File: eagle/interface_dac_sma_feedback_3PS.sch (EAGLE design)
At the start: 36 parts, among them IC1 ISO1540, IC2 LT1352PA, IC3 LT1352PA, Q1 TIP122V, Q2 TIP122V, Q3 TIP122V, X1 BU-SMA-V

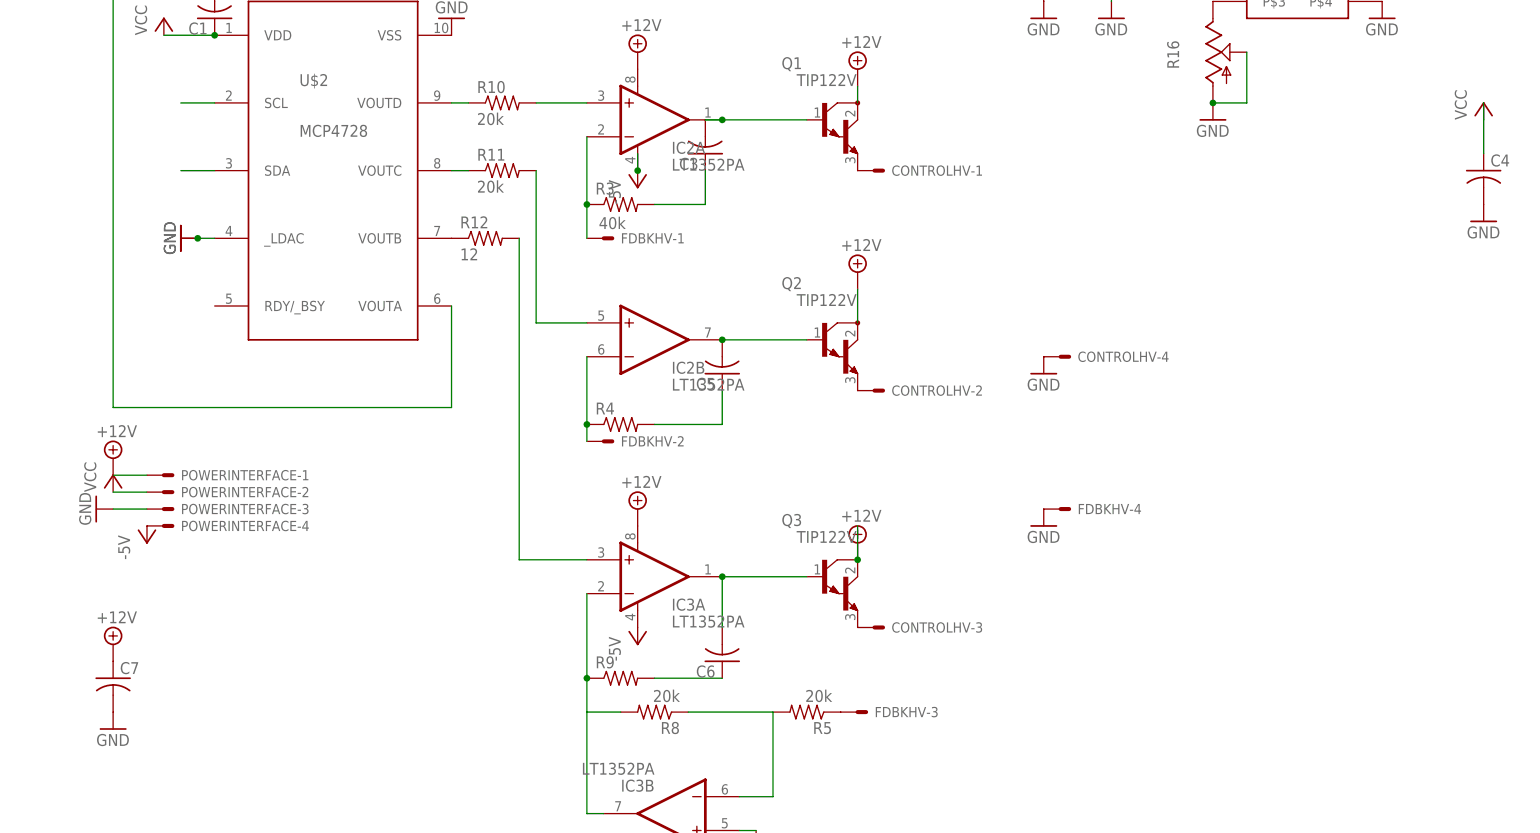
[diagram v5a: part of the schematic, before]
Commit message: update component values
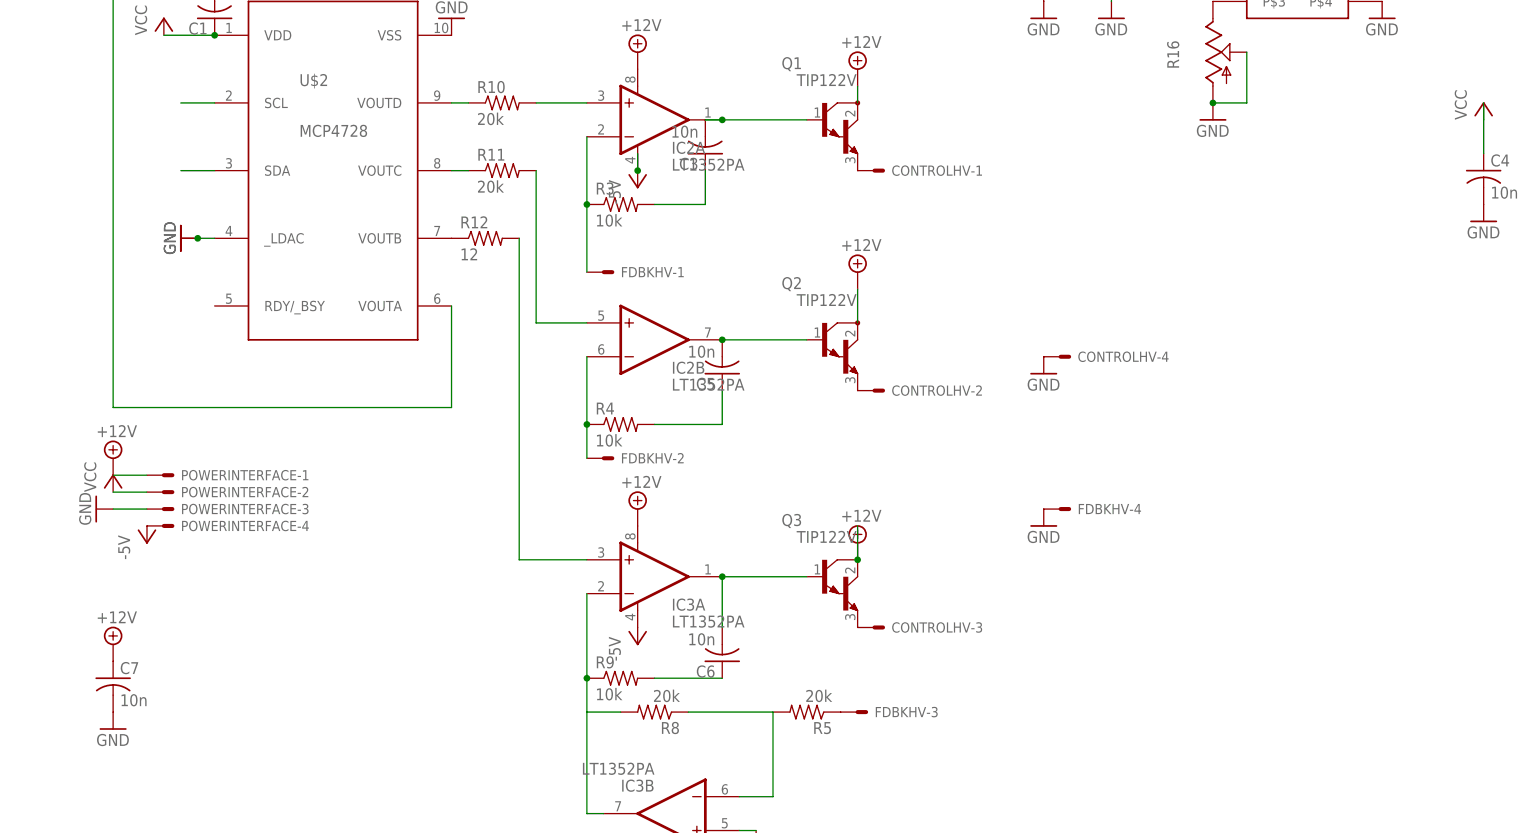
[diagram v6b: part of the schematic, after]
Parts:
- C3, C4, C5, C6, C7: value (none) -> 10n
- FDBKHV: value 40k -> (none)
- R3, R4, R9: value (none) -> 10k
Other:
- moved on the sheet: FDBKHV-1, FDBKHV-2
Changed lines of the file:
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@@
 <part name="P+2" library="supply2" deviceset="+12V" device=""/>
 <part name="U$1" library="linear-technology" deviceset="LTC6992" device=""/>
-<part name="C4" library="resistor" deviceset="C-US" device="075-063X106"/>
+<part name="C4" library="resistor" deviceset="C-US" device="075-063X106" value="10n"/>
 <part name="R16" library="pot" deviceset="TRIM_US-" device="B90P"/>
 <part name="GND13" library="supply1" deviceset="GND" device=""/>
@@
 <part name="P+8" library="supply2" deviceset="+12V" device=""/>
 <part name="CONTROLHV" library="con-molex" deviceset="KK-156-4" device=""/>
-<part name="FDBKHV" library="con-molex" deviceset="KK-156-4" device="" value="40k"/>
+<part name="FDBKHV" library="con-molex" deviceset="KK-156-4" device=""/>
 <part name="GND2" library="supply1" deviceset="GND" device=""/>
 <part name="GND6" library="supply1" deviceset="GND" device=""/>
@@
 <part name="P-2" library="supply1" deviceset="-5V" device=""/>
 <part name="GND18" library="supply1" deviceset="GND" device=""/>
-<part name="R3" library="resistor" deviceset="R-US_" device="0207/12"/>
-<part name="C3" library="resistor" deviceset="C-US" device="050-024X044"/>
-<part name="R4" library="resistor" deviceset="R-US_" device="0207/12"/>
-<part name="C5" library="resistor" deviceset="C-US" device="050-024X044"/>
-<part name="R9" library="resistor" deviceset="R-US_" device="0207/12"/>
-<part name="C6" library="resistor" deviceset="C-US" device="050-024X044"/>
+<part name="R3" library="resistor" deviceset="R-US_" device="0207/12" value="10k"/>
+<part name="C3" library="resistor" deviceset="C-US" device="050-024X044" value="10n"/>
+<part name="R4" library="resistor" deviceset="R-US_" device="0207/12" value="10k"/>
+<part name="C5" library="resistor" deviceset="C-US" device="050-024X044" value="10n"/>
+<part name="R9" library="resistor" deviceset="R-US_" device="0207/12" value="10k"/>
+<part name="C6" library="resistor" deviceset="C-US" device="050-024X044" value="10n"/>
 <part name="P+14" library="supply2" deviceset="+12V" device=""/>
-<part name="C7" library="resistor" deviceset="C-US" device="050-050X075"/>
+<part name="C7" library="resistor" deviceset="C-US" device="050-050X075" value="10n"/>
 <part name="GND20" library="supply1" deviceset="GND" device=""/>
 <part name="R10" library="resistor" deviceset="R-US_" device="0207/12" value="20k"/>
@@
 <instance part="CONTROLHV" gate="-3" x="203.2" y="15.24"/>
 <instance part="CONTROLHV" gate="-4" x="231.14" y="55.88"/>
-<instance part="FDBKHV" gate="-1" x="162.56" y="73.66"/>
-<instance part="FDBKHV" gate="-2" x="162.56" y="43.18"/>
+<instance part="FDBKHV" gate="-1" x="162.56" y="68.58"/>
+<instance part="FDBKHV" gate="-2" x="162.56" y="40.64"/>
 <instance part="FDBKHV" gate="-3" x="200.66" y="2.54"/>
 <instance part="FDBKHV" gate="-4" x="231.14" y="33.02"/>
@@
 <pinref part="FDBKHV" gate="-1" pin="S"/>
 <pinref part="R3" gate="G$1" pin="1"/>
-<wire x1="160.02" y1="78.74" x2="160.02" y2="73.66" width="0.1524" layer="91"/>
+<wire x1="160.02" y1="78.74" x2="160.02" y2="68.58" width="0.1524" layer="91"/>
 <junction x="160.02" y="78.74"/>
 <pinref part="IC2" gate="A" pin="-IN"/>
@@
 <pinref part="FDBKHV" gate="-2" pin="S"/>
 <pinref part="R4" gate="G$1" pin="1"/>
-<wire x1="160.02" y1="45.72" x2="160.02" y2="43.18" width="0.1524" layer="91"/>
+<wire x1="160.02" y1="45.72" x2="160.02" y2="40.64" width="0.1524" layer="91"/>
 <junction x="160.02" y="45.72"/>
 <pinref part="IC2" gate="B" pin="-IN"/>

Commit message: Update values, code
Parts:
- R10, R11: value 20k -> 10k
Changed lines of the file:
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@@
 <part name="C7" library="resistor" deviceset="C-US" device="050-050X075" value="10n"/>
 <part name="GND20" library="supply1" deviceset="GND" device=""/>
-<part name="R10" library="resistor" deviceset="R-US_" device="0207/12" value="20k"/>
-<part name="R11" library="resistor" deviceset="R-US_" device="0207/12" value="20k"/>
+<part name="R10" library="resistor" deviceset="R-US_" device="0207/12" value="10k"/>
+<part name="R11" library="resistor" deviceset="R-US_" device="0207/12" value="10k"/>
 <part name="R12" library="resistor" deviceset="R-US_" device="0207/12" value="12"/>
 <part name="Q1" library="transistor-npn" deviceset="TIP122*" device="V"/>

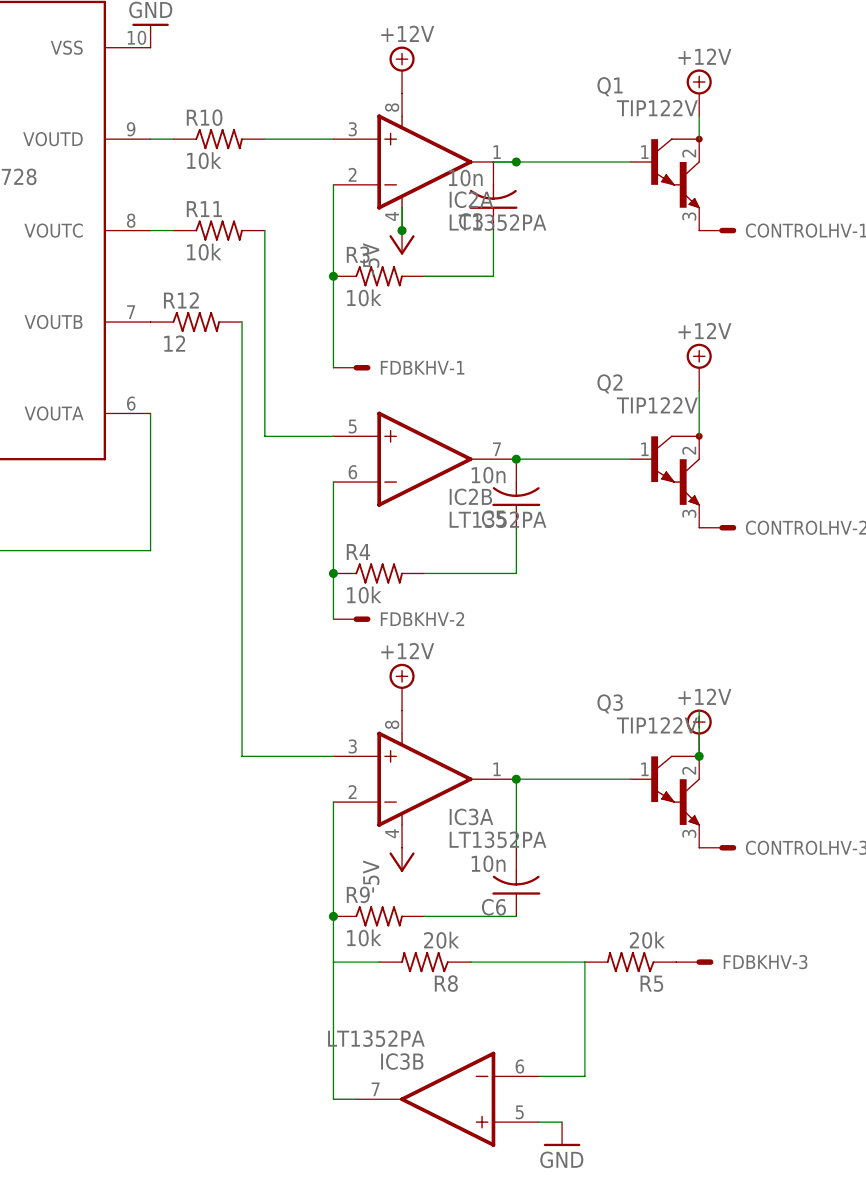
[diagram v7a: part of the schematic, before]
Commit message: Fix negative rail problems
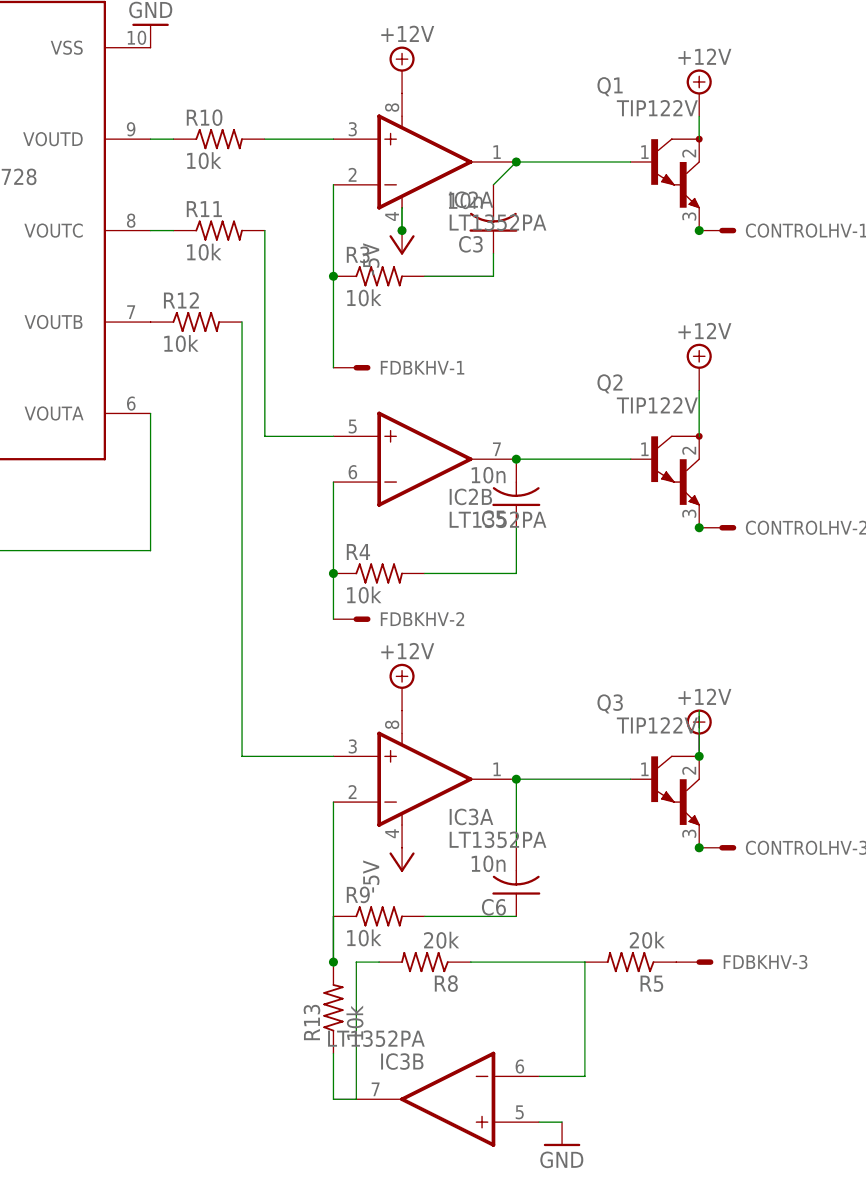
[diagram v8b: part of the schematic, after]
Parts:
- added R13: 10k, resistor:R-US_0207/12
- R12: value 12 -> 10k
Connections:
- new net N$27: IC3A.-IN, R13.2, R9.1
- net N$14: now also R13.1; no longer IC3A.-IN, R9.1
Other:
- moved on the sheet: C3
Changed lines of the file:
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@@
 <part name="R10" library="resistor" deviceset="R-US_" device="0207/12" value="10k"/>
 <part name="R11" library="resistor" deviceset="R-US_" device="0207/12" value="10k"/>
-<part name="R12" library="resistor" deviceset="R-US_" device="0207/12" value="12"/>
+<part name="R12" library="resistor" deviceset="R-US_" device="0207/12" value="10k"/>
 <part name="Q1" library="transistor-npn" deviceset="TIP122*" device="V"/>
 <part name="Q2" library="transistor-npn" deviceset="TIP122*" device="V"/>
@@
 <part name="IC3" library="linear-technology" deviceset="LT1352" device="PA"/>
 <part name="P-3" library="supply1" deviceset="-5V" device=""/>
+<part name="R13" library="resistor" deviceset="R-US_" device="0207/12" value="10k"/>
 </parts>
 <sheets>
@@
 <instance part="GND18" gate="1" x="185.42" y="-17.78"/>
 <instance part="R3" gate="G$1" x="165.1" y="78.74"/>
-<instance part="C3" gate="G$1" x="177.8" y="86.36" rot="R180"/>
+<instance part="C3" gate="G$1" x="177.8" y="83.82" rot="R180"/>
 <instance part="R4" gate="G$1" x="165.1" y="45.72"/>
 <instance part="C5" gate="G$1" x="180.34" y="53.34" rot="R180"/>
@@
 <instance part="IC3" gate="B" x="172.72" y="-12.7" rot="R180"/>
 <instance part="P-3" gate="1" x="167.64" y="81.28"/>
+<instance part="R13" gate="G$1" x="160.02" y="-2.54" rot="R90"/>
 </instances>
 <busses>
@@
 <segment>
 <wire x1="162.56" y1="-12.7" x2="160.02" y2="-12.7" width="0.1524" layer="91"/>
-<wire x1="160.02" y1="-12.7" x2="160.02" y2="2.54" width="0.1524" layer="91"/>
+<pinref part="IC3" gate="B" pin="OUT"/>
 <pinref part="R8" gate="G$1" pin="2"/>
-<wire x1="160.02" y1="2.54" x2="160.02" y2="7.62" width="0.1524" layer="91"/>
-<wire x1="160.02" y1="7.62" x2="160.02" y2="20.32" width="0.1524" layer="91"/>
-<wire x1="165.1" y1="2.54" x2="160.02" y2="2.54" width="0.1524" layer="91"/>
-<pinref part="R9" gate="G$1" pin="1"/>
-<junction x="160.02" y="7.62"/>
-<pinref part="IC3" gate="A" pin="-IN"/>
-<pinref part="IC3" gate="B" pin="OUT"/>
+<wire x1="165.1" y1="2.54" x2="162.56" y2="2.54" width="0.1524" layer="91"/>
+<wire x1="162.56" y1="2.54" x2="162.56" y2="-12.7" width="0.1524" layer="91"/>
+<pinref part="R13" gate="G$1" pin="1"/>
+<wire x1="160.02" y1="-12.7" x2="160.02" y2="-7.62" width="0.1524" layer="91"/>
 </segment>
 </net>
@@
 <wire x1="193.04" y1="91.44" x2="180.34" y2="91.44" width="0.1524" layer="91"/>
 <pinref part="C3" gate="G$1" pin="2"/>
-<wire x1="180.34" y1="91.44" x2="177.8" y2="91.44" width="0.1524" layer="91"/>
+<wire x1="180.34" y1="91.44" x2="177.8" y2="88.9" width="0.1524" layer="91"/>
 <pinref part="Q1" gate="G$1" pin="B"/>
 <pinref part="IC2" gate="A" pin="OUT"/>
@@
 <pinref part="CONTROLHV" gate="-1" pin="S"/>
 <pinref part="Q1" gate="G$1" pin="E"/>
+<junction x="200.66" y="83.82"/>
 </segment>
 </net>
@@
 <pinref part="C3" gate="G$1" pin="1"/>
 <wire x1="170.18" y1="78.74" x2="177.8" y2="78.74" width="0.1524" layer="91"/>
-<wire x1="177.8" y1="78.74" x2="177.8" y2="83.82" width="0.1524" layer="91"/>
+<wire x1="177.8" y1="78.74" x2="177.8" y2="81.28" width="0.1524" layer="91"/>
 </segment>
 </net>
@@
 <pinref part="CONTROLHV" gate="-3" pin="S"/>
 <pinref part="Q3" gate="G$1" pin="E"/>
+<junction x="200.66" y="15.24"/>
 </segment>
 </net>
@@
 <pinref part="Q2" gate="G$1" pin="E"/>
 <pinref part="CONTROLHV" gate="-2" pin="S"/>
-</segment>
-</net>
+<junction x="200.66" y="50.8"/>
+</segment>
+</net>
+<net name="N$27" class="0">
+<segment>
+<pinref part="IC3" gate="A" pin="-IN"/>
+<wire x1="160.02" y1="2.54" x2="160.02" y2="20.32" width="0.1524" layer="91"/>
+<pinref part="R9" gate="G$1" pin="1"/>
+<junction x="160.02" y="2.54"/>
+<pinref part="R13" gate="G$1" pin="2"/>
+<wire x1="160.02" y1="2.54" x2="160.02" y2="7.62" width="0.1524" layer="91"/>
+</segment>
+</net>
